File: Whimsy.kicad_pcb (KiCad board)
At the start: 2 copper layers, 281 x 88.1 mm, 100 parts, among them J1 OLED, J2 LED Breakout, K1 KEYSW, K10 KEYSW, K11 KEYSW, K12 KEYSW, K13 KEYSW, K14 KEYSW, K15 KEYSW, K16 KEYSW, K17 KEYSW, K18 KEYSW, K19 KEYSW, K2 KEYSW, K20 KEYSW, K21 KEYSW, K22 KEYSW, K23 KEYSW, K24 KEYSW, K25 KEYSW, K26 KEYSW, K27 KEYSW, K28 KEYSW, K29 KEYSW, K3 KEYSW, K30 KEYSW, K31 KEYSW, K32 KEYSW, K33 KEYSW, K34 KEYSW, K35 KEYSW, K36 KEYSW, K37 KEYSW, K38 KEYSW, K39 KEYSW, K4 KEYSW, K40 KEYSW, K41 KEYSW, K42 KEYSW, K43 KEYSW, K44 KEYSW, K45 KEYSW, K46 KEYSW, K47 KEYSW, K5 KEYSW, K6 KEYSW, K7 KEYSW, K8 KEYSW, K9 KEYSW, SW1 Rotary_Encoder_Switch, SW2 SW_PUSH, U1 ProMicro

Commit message: properly laid out keys, cut edges
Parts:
- K2, K20, K28, K46: footprint keebs:Mx_Alps_100 -> keebs:Mx_Alps_125
- K3, K45: footprint keebs:Mx_Alps_100 -> keebs:Mx_Alps_150
- moved J2 53.2 mm to (40.5, 76.2), turned to 180 degrees
- moved SW2 19.2 mm to (28.6, 121.4)
- moved K7 16.8 mm to (238.1, 107.2)
- moved K11 14.5 mm to (219.1, 107.2)
- moved K3 14.5 mm to (261.9, 107.2)
- moved K41 14.5 mm to (76.2, 69.1)
- moved K37 12.1 mm to (95.2, 69.1)
- moved K45 12.1 mm to (52.4, 69.1)
- moved K15 12.1 mm to (200.0, 107.2)
- moved K2 11.9 mm to (264.3, 88.1)
- moved K6 11.9 mm to (242.9, 88.1)
- moved K4 10.6 mm to (266.7, 126.2)
- moved K1 9.82 mm to (266.7, 69.1)
- moved K19 9.82 mm to (181.0, 107.2)
- moved SW1 9.82 mm to (28.6, 109.5)
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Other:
- board size 281 x 88.1 mm -> 261.9 x 81 mm

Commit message: added all diodes, new render, all cut corners
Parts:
- added TH1: HOLE, SofleKeyboard-footprint:M2_HOLE_PCB, F.Cu at (35.7, 100.0)
- added TH1: HOLE, SofleKeyboard-footprint:M2_HOLE_PCB, F.Cu at (21.4, 100.0)
- moved D1 191.9 mm to (275.6, 69.1), turned to 90 degrees
- moved D4 183.1 mm to (275.6, 126.2), turned to 90 degrees
- moved D6 172.8 mm to (251.8, 88.1), turned to 90 degrees
- moved D3 165.5 mm to (270.8, 107.2), turned to 90 degrees
- moved D5 161.6 mm to (256.5, 69.1), turned to 90 degrees
- moved D7 154.9 mm to (247.0, 107.2), turned to 90 degrees
- moved D2 151.8 mm to (273.2, 88.1), turned to 90 degrees
- moved D9 145.9 mm to (237.5, 69.1), turned to 90 degrees
- moved D21 126.1 mm to (180.3, 69.1), turned to 90 degrees
- moved D8 124.7 mm to (256.5, 126.2), turned to 90 degrees
- moved D13 121.5 mm to (218.4, 69.1), turned to 90 degrees
- moved D10 118.5 mm to (232.7, 88.1), turned to 90 degrees
- moved D17 112.2 mm to (199.4, 69.1), turned to 90 degrees
- moved D22 111.0 mm to (175.6, 88.1), turned to 90 degrees
- moved D45 110.0 mm to (61.3, 69.1), turned to 90 degrees
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
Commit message: started routing traces, finishing rev0.1
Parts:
- removed the TH1 at (35.7, 100.0)
- removed the TH1 at (21.4, 100.0)
- added TH1: HOLE, SofleKeyboard-footprint:M2_HOLE_PCB, F.Cu at (273.8, 100.0)
- added TH1: HOLE, SofleKeyboard-footprint:M2_HOLE_PCB, F.Cu at (259.6, 100.0)
- D1, D10, D11, D12, D13, D14, D15, D16, D17, D18, D19, D2, D20, D21, D22, D23, D24, D25, D26, D27, D28, D29, D3, D30, D31, D32, D33, D34, D35, D36, D37, D38, D39, D4, D40, D41, D42, D43, D44, D45, D46, D47, D48, D5, D6, D7, D8, D9: footprint SofleKeyboard-footprint:Diode_SOD123 -> Keebio-Parts:Diode-Hybrid-Back
- moved J1 240.4 mm to (264.1, 94.5)
- moved D1 238.8 mm to (36.8, 69.1), turned to 270 degrees
- moved D4 238.8 mm to (36.8, 126.2)
- moved D48 238.1 mm to (266.7, 124.9)
- moved K1 238.1 mm to (28.6, 69.1)
- moved K4 238.1 mm to (28.6, 126.2)
- moved SW1 238.1 mm to (266.7, 114.3)
- moved U1 238.1 mm to (266.7, 76.0)
- moved D2 234.0 mm to (39.2, 88.1)
- moved K2 233.4 mm to (31.0, 88.1)
- moved D3 229.2 mm to (41.6, 107.2)
- moved K3 228.6 mm to (33.3, 107.2)
- moved J2 217.2 mm to (255.9, 97.0)
- moved D5 200.7 mm to (55.9, 69.1), turned to 270 degrees
- moved D8 200.7 mm to (55.9, 126.2)
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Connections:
- K10 pad 2: Net-(K10-Pad2) -> Net-(D10-Pad2)
- K40 pad 2: Net-(K40-Pad2) -> Net-(D40-Pad2)
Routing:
- net col0: track 0.00 -> 394.9 mm, vias 0 -> 1
- net row3: track 0.00 -> 340.2 mm
- net row1: track 0.00 -> 290.2 mm, vias 0 -> 1
- net row0: track 0.00 -> 281.3 mm, vias 0 -> 1
- net row2: track 0.00 -> 280.0 mm, vias 0 -> 1
- net row7: track 0.00 -> 158.2 mm
- net col5: track 0.00 -> 154.1 mm
- net col1: track 0.00 -> 138.1 mm
- net col3: track 0.00 -> 136.7 mm
- net col2: track 0.00 -> 136.4 mm
- net col4: track 0.00 -> 136.2 mm
- net row6: track 0.00 -> 132.0 mm
- net row5: track 0.00 -> 124.2 mm
- net row4: track 0.00 -> 120.3 mm
- net Net-(D45-Pad2): track 0.00 -> 14.3 mm
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- added copper zone on F.Cu, net (none)
- added copper zone on B.Cu, net /GND
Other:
- board text added: "Prkns | https://prkns.me"
- board text added: "Whimsy | rev0.1"

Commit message: better routing, columns, rows and via's to connect to the elite c
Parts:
- removed SW2: SW_PUSH, SofleKeyboard-footprint:TACT_SWITCH_TVBP06
- U1: value ProMicro -> Elite-C; footprint Keebio-Parts:Elite-C -> Keebio-Parts:Elite-C-NoSilk
- moved D24 20.8 mm to (119.1, 126.2), turned to 270 degrees
- moved D28 20.2 mm to (157.2, 126.2), turned to 270 degrees
- moved D11 17.8 mm to (66.7, 107.2), turned to 270 degrees
- moved D15 17.8 mm to (85.7, 107.2), turned to 270 degrees
- moved D19 17.8 mm to (104.8, 107.2), turned to 270 degrees
- moved D27 17.8 mm to (142.9, 107.2), turned to 270 degrees
- moved D31 17.8 mm to (161.9, 107.2), turned to 270 degrees
- moved D32 17.8 mm to (181.0, 126.2), turned to 270 degrees
- moved D35 17.8 mm to (181.0, 107.2), turned to 270 degrees
- moved D36 17.8 mm to (200.0, 126.2), turned to 270 degrees
- moved D39 17.8 mm to (200.0, 107.2), turned to 270 degrees
- moved D43 17.8 mm to (219.1, 107.2), turned to 270 degrees
- moved D7 17.8 mm to (47.6, 107.2), turned to 270 degrees
- moved D23 17.8 mm to (123.8, 107.2), turned to 270 degrees
- moved D40 17.8 mm to (219.1, 126.2), turned to 270 degrees
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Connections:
- net /rot0 renamed Net-(U1-Pad1)
- net /rot1 renamed Net-(U1-Pad2)
- SW1 pad A: /Whimsy Matrix/rot0 -> rot0
- SW1 pad B: /Whimsy Matrix/rot1 -> rot1
- U1 pad 10: col3 -> row5
- U1 pad 11: col4 -> row2
- U1 pad 12: col5 -> row6
- U1 pad 13: row7 -> col0
- U1 pad 14: row6 -> col1
- U1 pad 15: row5 -> col2
- U1 pad 16: row4 -> col3
- U1 pad 17: row3 -> col4
- U1 pad 18: row2 -> col5
- U1 pad 19: row1 -> Net-(U1-Pad19)
- U1 pad 20: row0 -> Net-(U1-Pad20)
- U1 pad 22: reset -> Net-(U1-Pad22)
- U1 pad 25: (no net) -> row3
- U1 pad 26: (no net) -> row7
- U1 pad 27: (no net) -> Net-(U1-Pad27)
- U1 pad 28: (no net) -> rot1
- U1 pad 29: (no net) -> rot0
- U1 pad 7: col0 -> row4
- U1 pad 8: col1 -> row0
- U1 pad 9: col2 -> row1
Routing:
- net col1: track 138.1 -> 358.8 mm
- net row3: track 340.2 -> 226.0 mm, vias 0 -> 1
- net row2: track 280.0 -> 195.8 mm
- net row1: track 290.2 -> 232.0 mm
- net row0: track 281.3 -> 225.2 mm
- net row6: track 132.0 -> 76.2 mm
- net +5V: track 0.00 -> 44.2 mm
- net VCC: track 0.00 -> 41.6 mm
- net row7: track 158.2 -> 123.8 mm, vias 0 -> 1
- net row5: track 124.2 -> 91.2 mm, vias 0 -> 1
- net row4: track 120.3 -> 90.5 mm, vias 0 -> 1
- net SDA: track 0.00 -> 25.2 mm
- net SCL: track 0.00 -> 24.7 mm, vias 0 -> 1
- net rot1: track 0.00 -> 22.2 mm, vias 0 -> 1
- net rot0: track 0.00 -> 19.4 mm, vias 0 -> 1
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
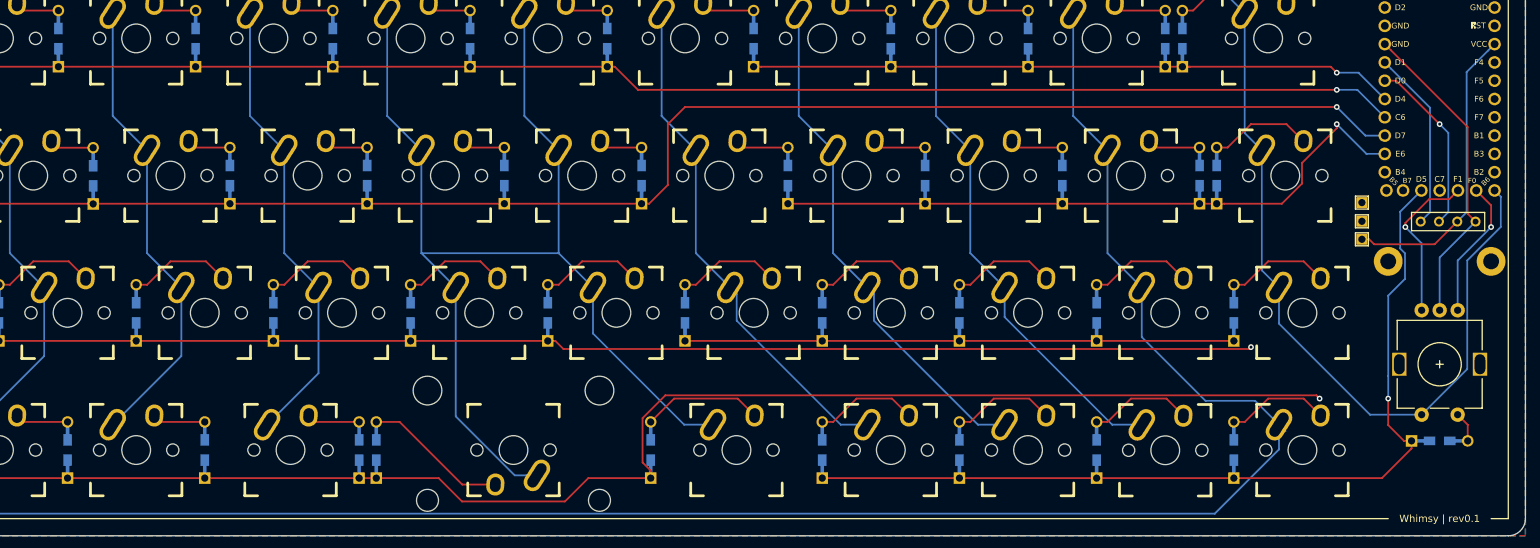
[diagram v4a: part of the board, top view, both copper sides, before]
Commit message: first fully routed/traced board
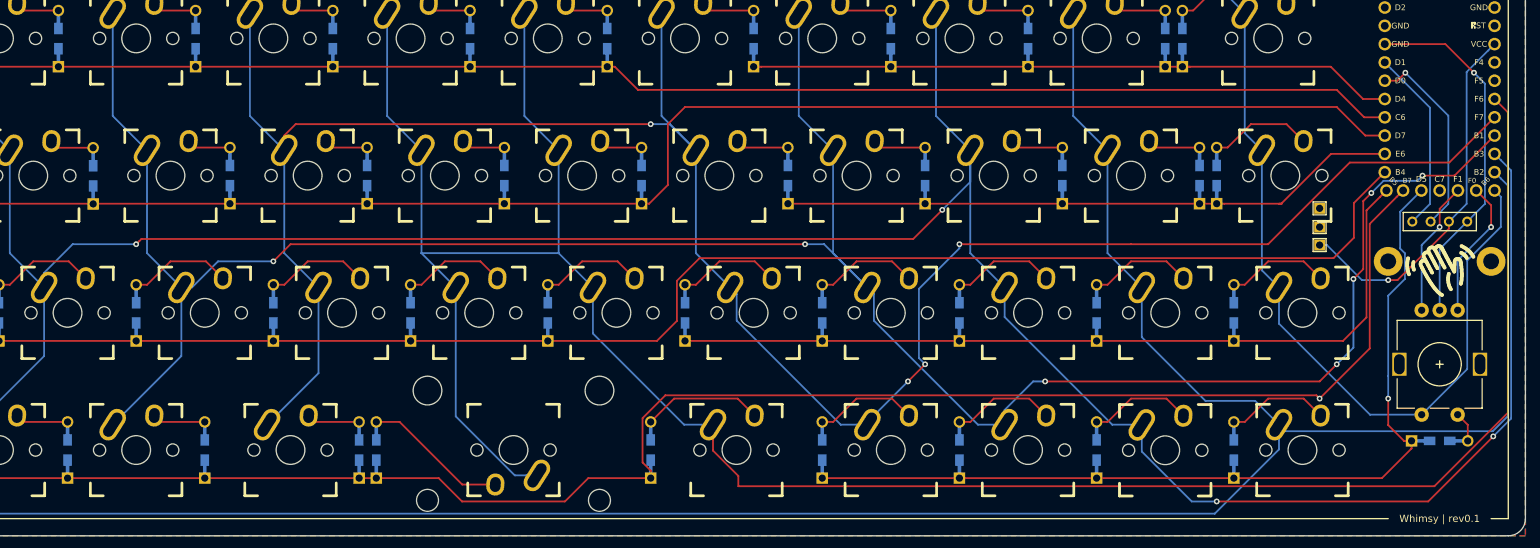
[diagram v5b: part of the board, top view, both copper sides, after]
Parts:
- added Wave: , CustomPrints:Wave, F.Cu at (261.9, 97.6)
- moved J2 5.93 mm to (250.0, 97.8)
- moved J1 1.16 mm to (262.9, 94.5)
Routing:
- net col2: track 136.4 -> 377.0 mm, vias 0 -> 4
- net col3: track 136.2 -> 333.4 mm, vias 0 -> 7
- net col4: track 135.2 -> 309.2 mm, vias 0 -> 4
- net col5: track 164.0 -> 329.4 mm
- net col1: track 358.8 -> 425.1 mm
- net row6: track 76.2 -> 114.7 mm
- net row2: track 195.8 -> 229.6 mm, vias 1 -> 0
- net row3: track 226.0 -> 259.7 mm
- net VCC: track 41.6 -> 51.2 mm, vias 0 -> 1
- net +5V: track 44.2 -> 50.2 mm, vias 0 -> 1
- net row5: track 91.2 -> 86.1 mm, vias 1 -> 0
- net rot1: track 22.2 -> 18.7 mm
- net SCL: track 24.7 -> 27.5 mm
- net row4: vias 1 -> 0
- net row1: vias 1 -> 0
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
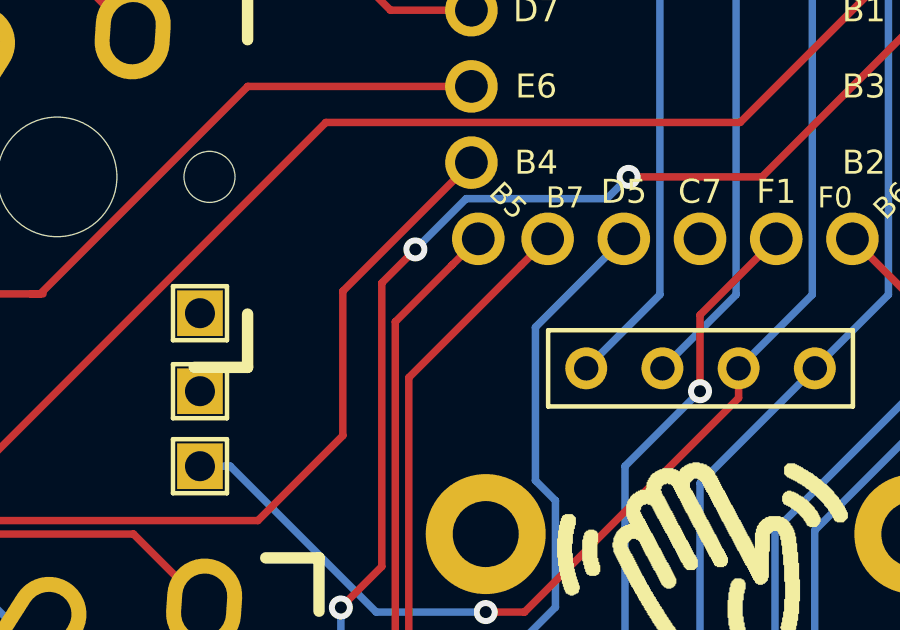
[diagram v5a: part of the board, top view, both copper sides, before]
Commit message: gnd pins were not working as inteded, solder mask was a little off, fixed overall matrix, tightened the schematic to make it more logical
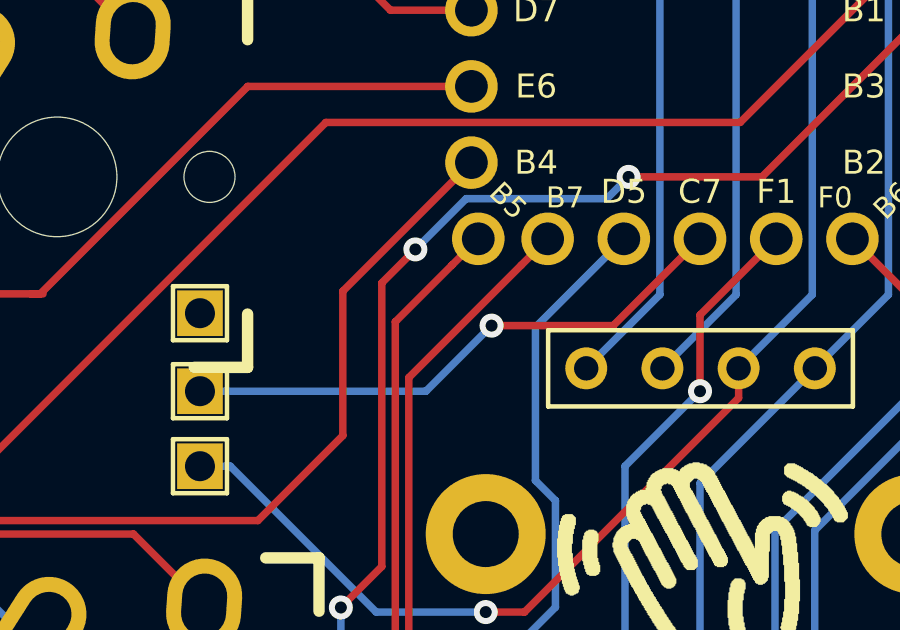
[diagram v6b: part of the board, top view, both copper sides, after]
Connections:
- J1 pad 4: +5V -> GND
- J2 pad 2: /LED -> LED
- J2 pad 3: /GND -> GND
- SW1 pad C: +5V -> GND
- U1 pad 23: +5V -> GND
- U1 pad 27: Net-(U1-Pad27) -> LED
- U1 pad 3: +5V -> GND
- U1 pad 4: +5V -> GND
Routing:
- net GND: track 0.00 -> 50.2 mm, vias 0 -> 1
- net +5V: track 50.2 -> 0.00 mm, vias 1 -> 0
- net LED: track 0.00 -> 18.8 mm, vias 0 -> 1
- added copper zone on B.Cu, net GND
- removed copper zone on B.Cu, net /GND

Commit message: flipped the elite-c, re-routed a lot of the board, tidied up some traces, new render, updated readme
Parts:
- U1: moved to B.Cu
- moved J2 2.38 mm to (252.4, 97.6)
- moved TH1 0.63 mm to (273.8, 100.6)
- moved TH1 0.63 mm to (259.6, 100.6)
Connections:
- U1 pad 13: col0 -> col3
- U1 pad 14: col1 -> col4
- U1 pad 15: col2 -> col0
- U1 pad 16: col3 -> col1
- U1 pad 17: col4 -> col2
- U1 pad 18: col5 -> row1
- U1 pad 19: Net-(U1-Pad19) -> row0
- U1 pad 20: Net-(U1-Pad20) -> row4
- U1 pad 25: row3 -> rot0
- U1 pad 26: row7 -> rot1
- U1 pad 28: rot1 -> row7
- U1 pad 29: rot0 -> row3
- U1 pad 7: row4 -> Net-(U1-Pad7)
- U1 pad 8: row0 -> Net-(U1-Pad8)
- U1 pad 9: row1 -> col5
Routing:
- net col2: track 377.0 -> 338.5 mm, vias 4 -> 2
- net col1: track 425.1 -> 397.1 mm
- net col3: track 333.4 -> 314.2 mm, vias 7 -> 4
- net col0: track 385.2 -> 366.7 mm
- net GND: track 50.2 -> 68.4 mm
- net col4: track 309.2 -> 291.2 mm, vias 4 -> 5
- net row6: track 114.7 -> 130.8 mm, vias 0 -> 2
- net row5: track 86.1 -> 101.0 mm
- net row2: track 229.6 -> 242.4 mm
- net col5: track 329.4 -> 324.6 mm
- net SDA: track 25.7 -> 30.5 mm, vias 0 -> 1
- net LED: track 18.8 -> 16.3 mm, vias 1 -> 0
- net row0: track 225.2 -> 223.1 mm
- net SCL: track 27.5 -> 25.6 mm
- net VCC: track 51.2 -> 53.0 mm, vias 1 -> 0
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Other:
- board text added: "Whimsy | rev0.2"
- board text removed: "Whimsy | rev0.1"
